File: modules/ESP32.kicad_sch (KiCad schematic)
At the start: 5 parts, among them U2 ESP32-C3-WROOM-02

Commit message: Adding source, source control
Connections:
- net ESP_RESET: now reaches C25.1, R13.1, U2.2 (EN)
- net ESP_RX: now reaches U2.11 (IO20/RXD)
- net ESP_TX: now reaches U2.12 (IO21/TXD)
- net ESP_BOOT: now reaches U2.18 (IO0)
- no-connect marks 9 -> 6
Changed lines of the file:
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@@
-	)
-	(no_connect
-		(at 114.3 72.39)
-	)
-	(no_connect
-		(at 144.78 69.85)
 	)
 	(no_connect
@@
 	)
 	(no_connect
-		(at 144.78 67.31)
-	)
-	(no_connect
 		(at 114.3 74.93)
 	)
@@
 	(wire
 		(pts
+			(xy 144.78 69.85) (xy 152.4 69.85)
+		)
+		(stroke
+			(width 0)
+			(type default)
+		)
+	)
+	(wire
+		(pts
 			(xy 105.41 55.88) (xy 105.41 54.61)
 		)
@@
 	(wire
 		(pts
+			(xy 107.95 72.39) (xy 114.3 72.39)
+		)
+		(stroke
+			(width 0)
+			(type default)
+		)
+	)
+	(wire
+		(pts
 			(xy 105.41 41.91) (xy 83.82 41.91)
 		)
@@
 	(wire
 		(pts
+			(xy 72.39 67.31) (xy 83.82 67.31)
+		)
+		(stroke
+			(width 0)
+			(type default)
+		)
+	)
+	(wire
+		(pts
 			(xy 83.82 41.91) (xy 83.82 55.88)
 		)
@@
 	(wire
 		(pts
+			(xy 144.78 67.31) (xy 152.4 67.31)
+		)
+		(stroke
+			(width 0)
+			(type default)
+		)
+	)
+	(wire
+		(pts
 			(xy 83.82 69.85) (xy 83.82 67.31)
 		)
@@
 			(width 0)
 			(type default)
+		)
+	)
+	(hierarchical_label "ESP_BOOT"
+		(shape input)
+		(at 107.95 72.39 180)
+		(effects
+			(font
+				(size 1.27 1.27)
+			)
+			(justify right)
+		)
+	)
+	(hierarchical_label "ESP_TX"
+		(shape output)
+		(at 152.4 69.85 0)
+		(effects
+			(font
+				(size 1.27 1.27)
+			)
+			(justify left)
+		)
+	)
+	(hierarchical_label "ESP_RESET"
+		(shape input)
+		(at 72.39 67.31 180)
+		(effects
+			(font
+				(size 1.27 1.27)
+			)
+			(justify right)
 		)
 	)
@@
 		)
 	)
+	(hierarchical_label "ESP_RX"
+		(shape input)
+		(at 152.4 67.31 0)
+		(effects
+			(font
+				(size 1.27 1.27)
+			)
+			(justify left)
+		)
+	)

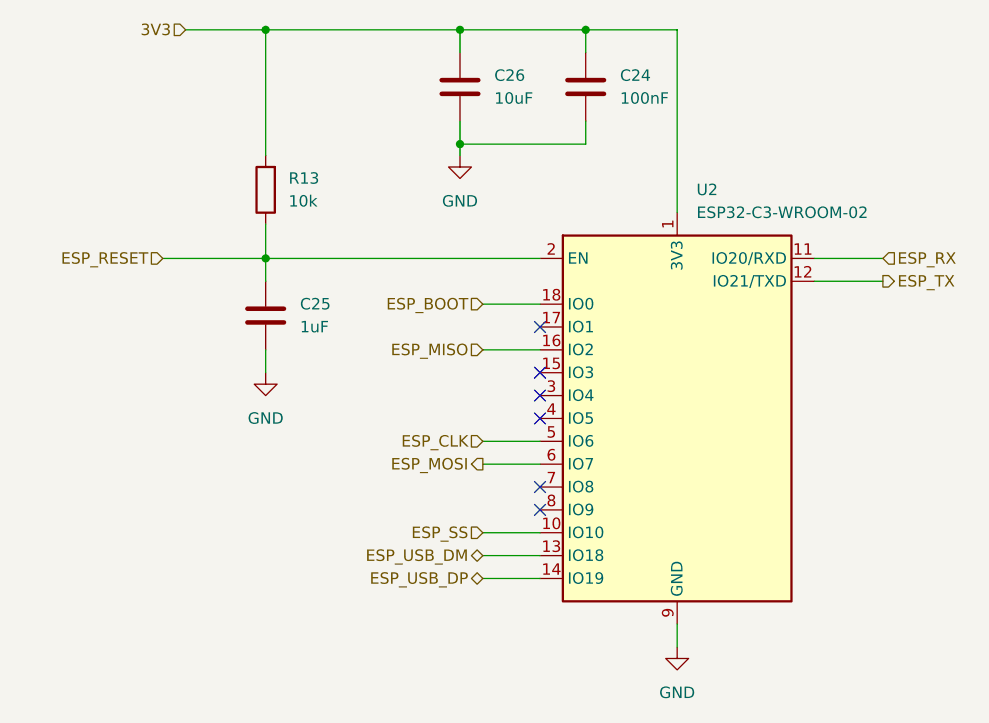
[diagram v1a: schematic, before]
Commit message: Modificaciond de conexiones
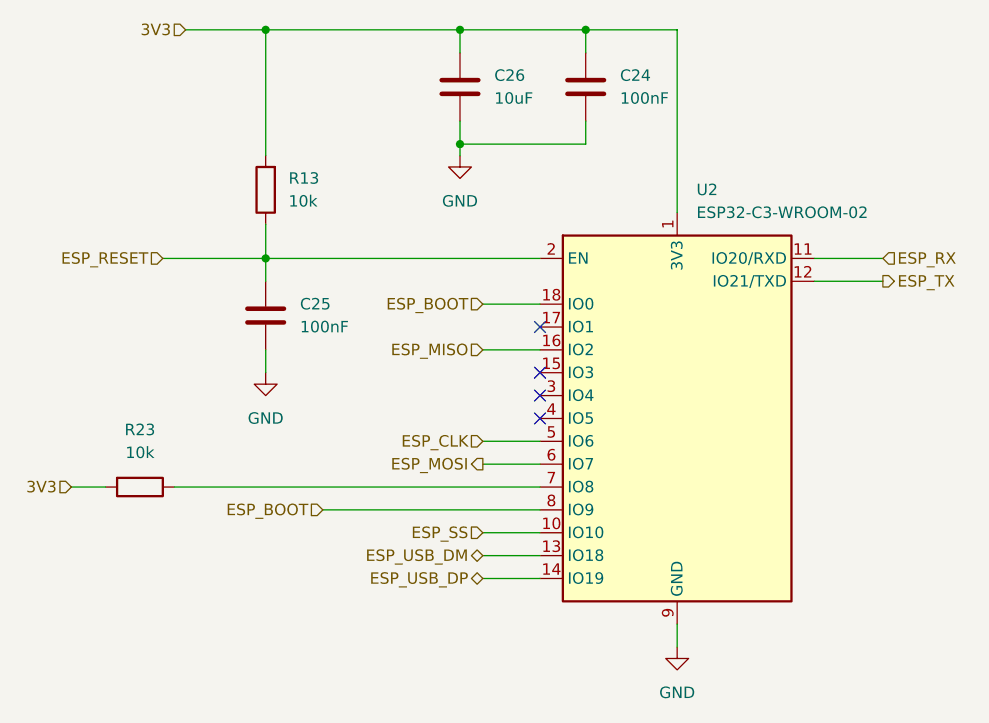
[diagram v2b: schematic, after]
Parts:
- added R23: 10k, Resistor_SMD:R_0603_1608Metric, symbol Device:R
- C24, C26: Provider (none) -> Digikey
- C25: value 1uF -> 100nF; footprint Capacitor_SMD:C_0603_1608Metric -> Capacitor_SMD:C_0402_1005Metric; Part Number CL10B105KP8NNNC -> CL05B104KA5NNNC
- U2: Part Number (none) -> ESP32-C3-WROOM-02-H4; Provider (none) -> Digikey
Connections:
- net 3V3: now also R23.2
- net ESP_BOOT: now also U2.8 (IO9)
- net at U2.7 (IO8): now also R23.1
- no-connect marks 6 -> 4
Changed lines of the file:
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@@
-	)
-	(no_connect
-		(at 114.3 92.71)
 	)
 	(no_connect
@@
 		(at 114.3 74.93)
 	)
-	(no_connect
-		(at 114.3 95.25)
-	)
 	(wire
 		(pts
@@
 	(wire
 		(pts
+			(xy 114.3 95.25) (xy 90.17 95.25)
+		)
+		(stroke
+			(width 0)
+			(type default)
+		)
+	)
+	(wire
+		(pts
 			(xy 119.38 54.61) (xy 119.38 52.07)
 		)
@@
 	(wire
 		(pts
+			(xy 73.66 92.71) (xy 114.3 92.71)
+		)
+		(stroke
+			(width 0)
+			(type default)
+		)
+	)
+	(wire
+		(pts
 			(xy 105.41 41.91) (xy 105.41 44.45)
 		)
@@
 		(pts
 			(xy 144.78 69.85) (xy 152.4 69.85)
+		)
+		(stroke
+			(width 0)
+			(type default)
+		)
+	)
+	(wire
+		(pts
+			(xy 62.23 92.71) (xy 66.04 92.71)
 		)
 		(stroke
@@
 		)
 	)
+	(hierarchical_label "ESP_BOOT"
+		(shape input)
+		(at 90.17 95.25 180)
+		(effects
+			(font
+				(size 1.27 1.27)
+			)
+			(justify right)
+		)
+	)
 	(hierarchical_label "ESP_TX"
 		(shape output)
@@
 		(shape bidirectional)
 		(at 107.95 100.33 180)
+		(effects
+			(font
+				(size 1.27 1.27)
+			)
+			(justify right)
+		)
+	)
+	(hierarchical_label "3V3"
+		(shape input)
+		(at 62.23 92.71 180)
 		(effects
 			(font
@@
 	(symbol
 		(lib_id "Device:C")
+		(at 83.82 73.66 0)
+		(unit 1)
+		(exclude_from_sim no)
+		(in_bom yes)
+		(on_board yes)
+		(dnp no)
+		(property "Reference" "C25"
+			(at 87.63 72.3899 0)
+			(effects
+				(font
+					(size 1.27 1.27)
+				)
+				(justify left)
+			)
+		)
+		(property "Value" "100nF"
+			(at 87.63 74.93 0)
+			(effects
+				(font
+					(size 1.27 1.27)
+				)
+				(justify left)
+			)
+		)
+		(property "Footprint" "Capacitor_SMD:C_0402_1005Metric"
+			(at 84.7852 77.47 0)
+			(effects
+				(font
+					(size 1.27 1.27)
+				)
+				(hide yes)
+			)
+		)
+		(property "Datasheet" "https://mm.digikey.com/Volume0/opasdata/d220001/medias/docus/729/CL05B104KA5NNNC_Spec.pdf"
+			(at 83.82 73.66 0)
+			(effects
+				(font
+					(size 1.27 1.27)
+				)
+				(hide yes)
+			)
+		)
+		(property "Description" "CAP CER 0.1UF 25V X7R 0402"
+			(at 83.82 73.66 0)
+			(effects
+				(font
+					(size 1.27 1.27)
+				)
+				(hide yes)
+			)
+		)
+		(property "Part Number" "CL05B104KA5NNNC"
+			(at 83.82 73.66 0)
+			(effects
+				(font
+					(size 1.27 1.27)
+				)
+				(hide yes)
+			)
+		)
+		(property "Provider" "Digikey"
+			(at 83.82 73.66 0)
+			(effects
+				(font
+					(size 1.27 1.27)
+				)
+				(hide yes)
+			)
+		)
+		(pin "1"
+		)
+		(pin "2"
+		)
+		(instances
+			(project "RP_devBoard"
+				(path "/3efb3214-cf20-4475-a403-c426a77bfef6/ae60b799-78d5-45ce-add1-9e61037e964b"
+					(reference "C25")
+					(unit 1)
+				)
+			)
+		)
+	)
+	(symbol
+		(lib_id "Device:C")
 		(at 105.41 48.26 0)
 		(unit 1)
@@
 			)
 		)
-		(property "Provider" ""
+		(property "Provider" "Digikey"
 			(at 105.41 48.26 0)
 			(effects
@@
 			)
 		)
-		(property "Provider" ""
+		(property "Provider" "Digikey"
 			(at 119.38 48.26 0)
 			(effects
@@
 	)
 	(symbol
-		(lib_id "Device:C")
-		(at 83.82 73.66 0)
+		(lib_id "Device:R")
+		(at 69.85 92.71 270)
 		(unit 1)
 		(exclude_from_sim no)
@@
 		(on_board yes)
 		(dnp no)
-		(property "Reference" "C25"
-			(at 87.63 72.3899 0)
-			(effects
-				(font
-					(size 1.27 1.27)
-				)
-				(justify left)
-			)
-		)
-		(property "Value" "1uF"
-			(at 87.63 74.93 0)
-			(effects
-				(font
-					(size 1.27 1.27)
-				)
-				(justify left)
-			)
-		)
-		(property "Footprint" "Capacitor_SMD:C_0603_1608Metric"
-			(at 84.7852 77.47 0)
-			(effects
-				(font
-					(size 1.27 1.27)
-				)
-				(hide yes)
-			)
-		)
-		(property "Datasheet" "https://mm.digikey.com/Volume0/opasdata/d220001/medias/docus/3584/CL10B105KP8NNNC_Spec.pdf"
-			(at 83.82 73.66 0)
-			(effects
-				(font
-					(size 1.27 1.27)
-				)
-				(hide yes)
-			)
-		)
-		(property "Description" "CAP CER 1UF 10V X7R 0603"
-			(at 83.82 73.66 0)
-			(effects
-				(font
-					(size 1.27 1.27)
-				)
-				(hide yes)
-			)
-		)
-		(property "Part Number" "CL10B105KP8NNNC"
-			(at 83.82 73.66 0)
+		(fields_autoplaced yes)
+		(property "Reference" "R23"
+			(at 69.85 86.36 90)
+			(effects
+				(font
+					(size 1.27 1.27)
+				)
+			)
+		)
+		(property "Value" "10k"
+			(at 69.85 88.9 90)
+			(effects
+				(font
+					(size 1.27 1.27)
+				)
+			)
+		)
+		(property "Footprint" "Resistor_SMD:R_0603_1608Metric"
+			(at 69.85 90.932 90)
+			(effects
+				(font
+					(size 1.27 1.27)
+				)
+				(hide yes)
+			)
+		)
+		(property "Datasheet" "https://yageogroup.com/content/datasheet/asset/file/PYU-RC_GROUP_51_ROHS_L"
+			(at 69.85 92.71 0)
+			(effects
+				(font
+					(size 1.27 1.27)
+				)
+				(hide yes)
+			)
+		)
+		(property "Description" "RES 10K OHM 1% 1/10W 0603"
+			(at 69.85 92.71 0)
+			(effects
+				(font
+					(size 1.27 1.27)
+				)
+				(hide yes)
+			)
+		)
+		(property "Part Number" "RC0603FR-0710KL"
+			(at 69.85 92.71 0)
 			(effects
 				(font
@@
 		)
 		(property "Provider" "Digikey"
-			(at 83.82 73.66 0)
+			(at 69.85 92.71 0)
 			(effects
 				(font
@@
 			(project "RP_devBoard"
 				(path "/3efb3214-cf20-4475-a403-c426a77bfef6/ae60b799-78d5-45ce-add1-9e61037e964b"
-					(reference "C25")
+					(reference "R23")
 					(unit 1)
 				)
@@
 			)
 		)
-		(property "Part Number" ""
+		(property "Part Number" "ESP32-C3-WROOM-02-H4"
 			(at 129.54 85.09 0)
 			(effects
@@
 			)
 		)
-		(property "Provider" ""
+		(property "Provider" "Digikey"
 			(at 129.54 85.09 0)
 			(effects

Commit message: correction of mikroBUS, USB on ESP32 and power mosfet
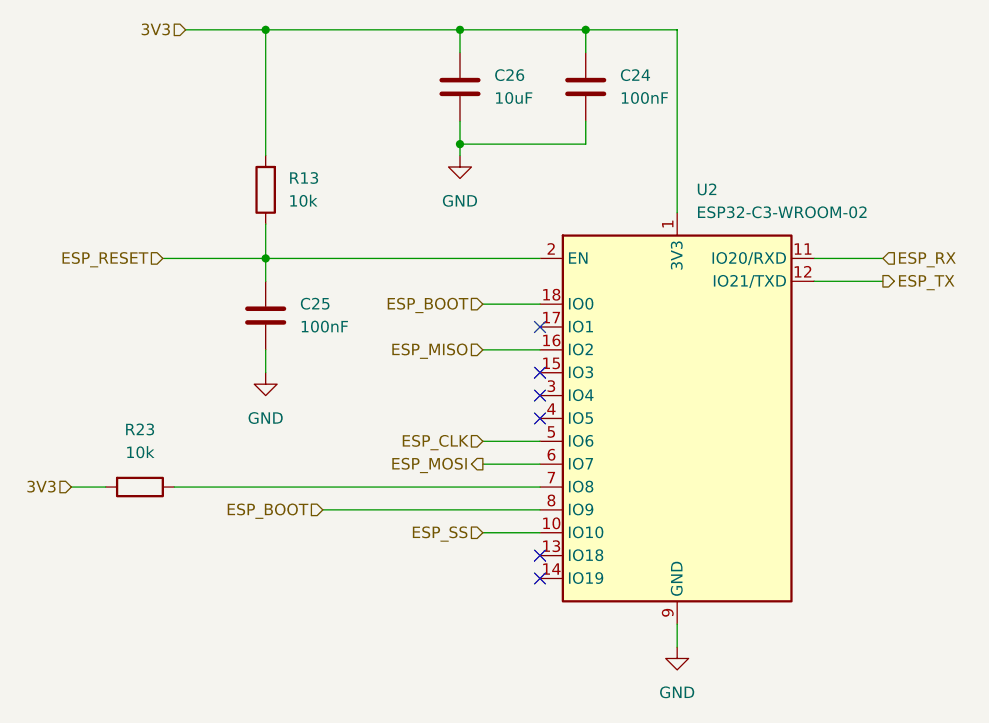
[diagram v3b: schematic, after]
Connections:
- net ESP_USB_DM: no longer names the net of U2.13 (IO18)
- net ESP_USB_DP: no longer names the net of U2.14 (IO19)
- no-connect marks 4 -> 6
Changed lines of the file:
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@@
 		(at 114.3 74.93)
 	)
+	(no_connect
+		(at 114.3 102.87)
+	)
+	(no_connect
+		(at 114.3 100.33)
+	)
 	(wire
 		(pts
@@
 	(wire
 		(pts
-			(xy 107.95 102.87) (xy 114.3 102.87)
-		)
-		(stroke
-			(width 0)
-			(type default)
-		)
-	)
-	(wire
-		(pts
 			(xy 83.82 80.01) (xy 83.82 77.47)
 		)
@@
 		(pts
 			(xy 129.54 110.49) (xy 129.54 107.95)
-		)
-		(stroke
-			(width 0)
-			(type default)
-		)
-	)
-	(wire
-		(pts
-			(xy 107.95 100.33) (xy 114.3 100.33)
 		)
 		(stroke
@@
 		)
 	)
-	(hierarchical_label "ESP_USB_DP"
-		(shape bidirectional)
-		(at 107.95 102.87 180)
+	(hierarchical_label "ESP_MISO"
+		(shape input)
+		(at 107.95 77.47 180)
 		(effects
 			(font
@@
 		)
 	)
-	(hierarchical_label "ESP_MISO"
-		(shape input)
-		(at 107.95 77.47 180)
-		(effects
-			(font
-				(size 1.27 1.27)
-			)
-			(justify right)
-		)
-	)
 	(hierarchical_label "ESP_CLK"
 		(shape input)
@@
 		(effects
 			(font
-				(size 1.27 1.27)
-			)
-			(justify right)
-		)
-	)
-	(hierarchical_label "ESP_USB_DM"
-		(shape bidirectional)
-		(at 107.95 100.33 180)
-		(effects
-			(font

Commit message: pcb power layout
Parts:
- added C36: 10uF, Capacitor_SMD:C_0603_1608Metric, symbol Device:C
- added R25: 10k, Resistor_SMD:R_0603_1608Metric, symbol Device:R
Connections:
- net 3V3: now also C36.1, R25.2
- net ESP_BOOT: now also R25.1; no longer U2.18 (IO0)
- net GND: now also C36.2
- no-connect marks 6 -> 7

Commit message: save
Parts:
- C24: footprint Capacitor_SMD:C_0402_1005Metric -> Capacitor_SMD:C_0603_1608Metric
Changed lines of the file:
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@@
 			)
 		)
-		(property "Footprint" "Capacitor_SMD:C_0402_1005Metric"
+		(property "Footprint" "Capacitor_SMD:C_0603_1608Metric"
 			(at 120.3452 52.07 0)
 			(effects

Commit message: Cambio de layout, correccion de pinout
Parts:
- C24: renamed from C25; footprint Capacitor_SMD:C_0402_1005Metric -> Capacitor_SMD:C_0603_1608Metric
- renumbered C36 to C25, C24 to C36, R23 to R13, R13 to R21, R25 to R23
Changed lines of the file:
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@@
 		(instances
 			(project "RP_devBoard"
-				(path "/3efb3214-cf20-4475-a403-c426a77bfef6/ae60b799-78d5-45ce-add1-9e61037e964b"
+				(path "/3efb3214-cf20-4475-a403-c426a77bfef6/7b15b1a5-e5ef-40fa-9d86-3d35cc14cf38"
 					(reference "#PWR039")
 					(unit 1)
@@
 		(on_board yes)
 		(dnp no)
-		(property "Reference" "C25"
+		(property "Reference" "C24"
 			(at 87.63 72.3899 0)
 			(effects
@@
 			)
 		)
-		(property "Footprint" "Capacitor_SMD:C_0402_1005Metric"
+		(property "Footprint" "Capacitor_SMD:C_0603_1608Metric"
 			(at 84.7852 77.47 0)
 			(effects
@@
 		(instances
 			(project "RP_devBoard"
-				(path "/3efb3214-cf20-4475-a403-c426a77bfef6/ae60b799-78d5-45ce-add1-9e61037e964b"
-					(reference "C25")
+				(path "/3efb3214-cf20-4475-a403-c426a77bfef6/7b15b1a5-e5ef-40fa-9d86-3d35cc14cf38"
+					(reference "C24")
 					(unit 1)
 				)
@@
 		(instances
 			(project "RP_devBoard"
-				(path "/3efb3214-cf20-4475-a403-c426a77bfef6/ae60b799-78d5-45ce-add1-9e61037e964b"
+				(path "/3efb3214-cf20-4475-a403-c426a77bfef6/7b15b1a5-e5ef-40fa-9d86-3d35cc14cf38"
 					(reference "C26")
 					(unit 1)
@@
 		(on_board yes)
 		(dnp no)
-		(property "Reference" "C36"
+		(property "Reference" "C25"
 			(at 96.52 46.9899 0)
 			(effects
@@
 		(instances
 			(project "RP_devBoard"
-				(path "/3efb3214-cf20-4475-a403-c426a77bfef6/ae60b799-78d5-45ce-add1-9e61037e964b"
-					(reference "C36")
+				(path "/3efb3214-cf20-4475-a403-c426a77bfef6/7b15b1a5-e5ef-40fa-9d86-3d35cc14cf38"
+					(reference "C25")
 					(unit 1)
 				)
@@
 		(on_board yes)
 		(dnp no)
-		(property "Reference" "C24"
+		(property "Reference" "C36"
 			(at 123.19 46.9899 0)
 			(effects
@@
 		(instances
 			(project "RP_devBoard"
-				(path "/3efb3214-cf20-4475-a403-c426a77bfef6/ae60b799-78d5-45ce-add1-9e61037e964b"
-					(reference "C24")
+				(path "/3efb3214-cf20-4475-a403-c426a77bfef6/7b15b1a5-e5ef-40fa-9d86-3d35cc14cf38"
+					(reference "C36")
 					(unit 1)
 				)
@@
 		(dnp no)
 		(fields_autoplaced yes)
-		(property "Reference" "R23"
+		(property "Reference" "R13"
 			(at 69.85 86.36 90)
 			(effects
@@
 		(instances
 			(project "RP_devBoard"
-				(path "/3efb3214-cf20-4475-a403-c426a77bfef6/ae60b799-78d5-45ce-add1-9e61037e964b"
-					(reference "R23")
+				(path "/3efb3214-cf20-4475-a403-c426a77bfef6/7b15b1a5-e5ef-40fa-9d86-3d35cc14cf38"
+					(reference "R13")
 					(unit 1)
 				)
@@
 		(instances
 			(project "RP_devBoard"
-				(path "/3efb3214-cf20-4475-a403-c426a77bfef6/ae60b799-78d5-45ce-add1-9e61037e964b"
+				(path "/3efb3214-cf20-4475-a403-c426a77bfef6/7b15b1a5-e5ef-40fa-9d86-3d35cc14cf38"
 					(reference "U2")
 					(unit 1)
@@
 		(dnp no)
 		(fields_autoplaced yes)
-		(property "Reference" "#PWR040"
+		(property "Reference" "#PWR034"
 			(at 83.82 86.36 0)
 			(effects
@@
 		(instances
 			(project "RP_devBoard"
-				(path "/3efb3214-cf20-4475-a403-c426a77bfef6/ae60b799-78d5-45ce-add1-9e61037e964b"
-					(reference "#PWR040")
+				(path "/3efb3214-cf20-4475-a403-c426a77bfef6/7b15b1a5-e5ef-40fa-9d86-3d35cc14cf38"
+					(reference "#PWR034")
 					(unit 1)
 				)
@@
 		(dnp no)
 		(fields_autoplaced yes)
-		(property "Reference" "R13"
+		(property "Reference" "R21"
 			(at 86.36 58.4199 0)
 			(effects
@@
 		(instances
 			(project "RP_devBoard"
-				(path "/3efb3214-cf20-4475-a403-c426a77bfef6/ae60b799-78d5-45ce-add1-9e61037e964b"
-					(reference "R13")
+				(path "/3efb3214-cf20-4475-a403-c426a77bfef6/7b15b1a5-e5ef-40fa-9d86-3d35cc14cf38"
+					(reference "R21")
 					(unit 1)
 				)
@@
 		(dnp no)
 		(fields_autoplaced yes)
-		(property "Reference" "R25"
+		(property "Reference" "R23"
 			(at 90.17 88.9 90)
 			(effects
@@
 		(instances
 			(project "RP_devBoard"
-				(path "/3efb3214-cf20-4475-a403-c426a77bfef6/ae60b799-78d5-45ce-add1-9e61037e964b"
-					(reference "R25")
+				(path "/3efb3214-cf20-4475-a403-c426a77bfef6/7b15b1a5-e5ef-40fa-9d86-3d35cc14cf38"
+					(reference "R23")
 					(unit 1)
 				)
@@
 		(dnp no)
 		(fields_autoplaced yes)
-		(property "Reference" "#PWR034"
+		(property "Reference" "#PWR040"
 			(at 129.54 116.84 0)
 			(effects
@@
 		)
 		(instances
-			(project ""
-				(path "/3efb3214-cf20-4475-a403-c426a77bfef6/ae60b799-78d5-45ce-add1-9e61037e964b"
-					(reference "#PWR034")
-					(unit 1)
-				)
+			(project "RP_devBoard"
+				(path "/3efb3214-cf20-4475-a403-c426a77bfef6/7b15b1a5-e5ef-40fa-9d86-3d35cc14cf38"
+					(reference "#PWR040")
+					(unit 1)
+				)

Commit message: finishing version 1.0
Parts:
- C24, C36: Part Number CL05B104KA5NNNC -> C0603C104K5RACTU
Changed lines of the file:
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@@
 			)
 		)
-		(property "Datasheet" "https://mm.digikey.com/Volume0/opasdata/d220001/medias/docus/729/CL05B104KA5NNNC_Spec.pdf"
-			(at 83.82 73.66 0)
-			(effects
-				(font
-					(size 1.27 1.27)
-				)
-				(hide yes)
-			)
-		)
-		(property "Description" "CAP CER 0.1UF 25V X7R 0402"
-			(at 83.82 73.66 0)
-			(effects
-				(font
-					(size 1.27 1.27)
-				)
-				(hide yes)
-			)
-		)
-		(property "Part Number" "CL05B104KA5NNNC"
+		(property "Datasheet" "https://yageogroup.com/content/datasheet/asset/file/KEM_C1002_X7R_SMD"
+			(at 83.82 73.66 0)
+			(effects
+				(font
+					(size 1.27 1.27)
+				)
+				(hide yes)
+			)
+		)
+		(property "Description" "CAP CER 0.1UF 50V X7R 0603"
+			(at 83.82 73.66 0)
+			(effects
+				(font
+					(size 1.27 1.27)
+				)
+				(hide yes)
+			)
+		)
+		(property "Part Number" "C0603C104K5RACTU"
 			(at 83.82 73.66 0)
 			(effects
@@
 			)
 		)
-		(property "Datasheet" "https://mm.digikey.com/Volume0/opasdata/d220001/medias/docus/729/CL05B104KA5NNNC_Spec.pdf"
+		(property "Datasheet" "https://yageogroup.com/content/datasheet/asset/file/KEM_C1002_X7R_SMD"
 			(at 119.38 48.26 0)
 			(effects
@@
 			)
 		)
-		(property "Description" "CAP CER 0.1UF 25V X7R 0402"
+		(property "Description" "CAP CER 0.1UF 50V X7R 0603"
 			(at 119.38 48.26 0)
 			(effects
@@
 			)
 		)
-		(property "Part Number" "CL05B104KA5NNNC"
+		(property "Part Number" "C0603C104K5RACTU"
 			(at 119.38 48.26 0)
 			(effects
